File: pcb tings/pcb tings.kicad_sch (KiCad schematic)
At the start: 24 parts, among them SW1 SW_Push, U1 ATmega32U4-A, Y1 16MHz

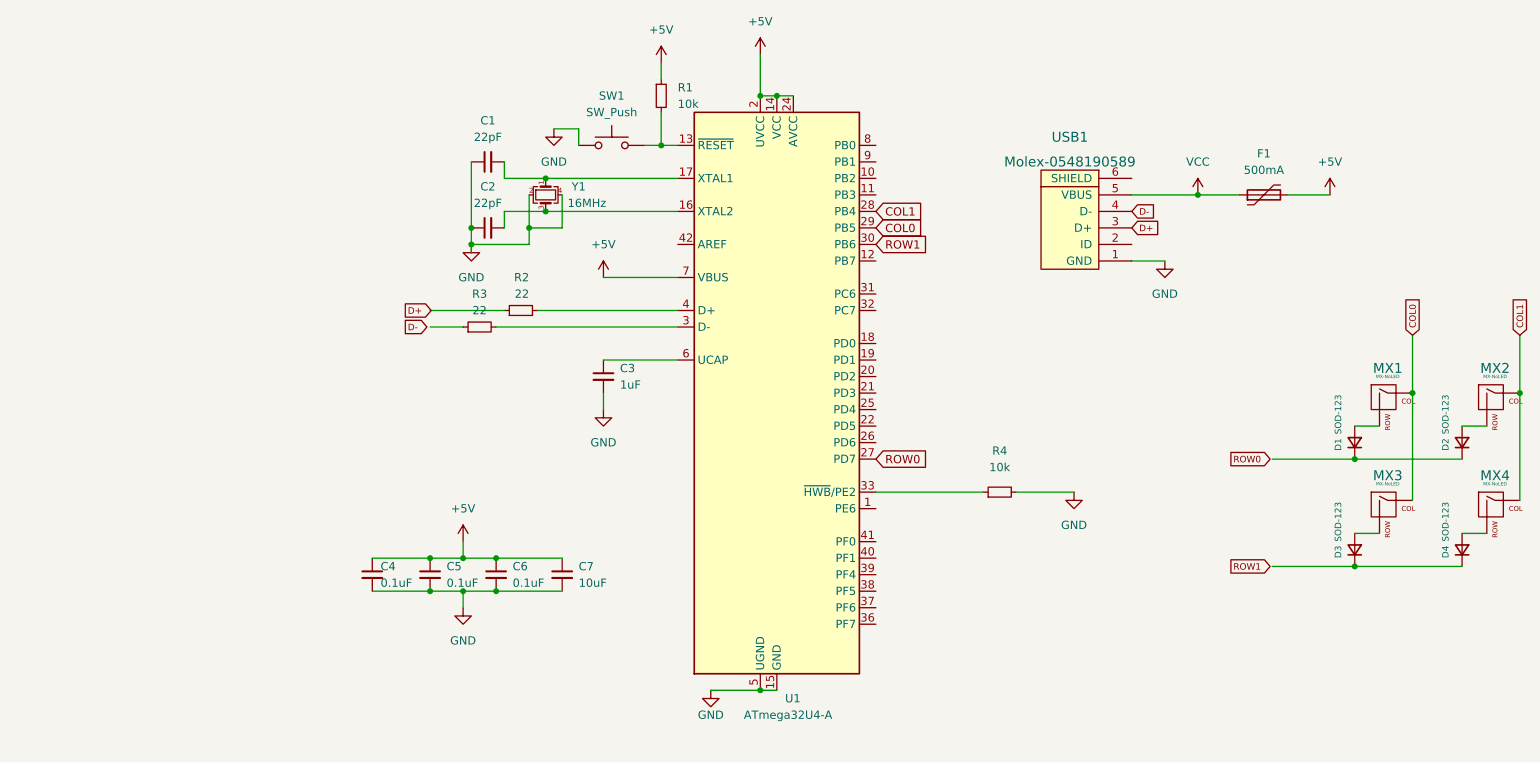
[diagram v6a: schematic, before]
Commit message: fixed connections (ratsnest)
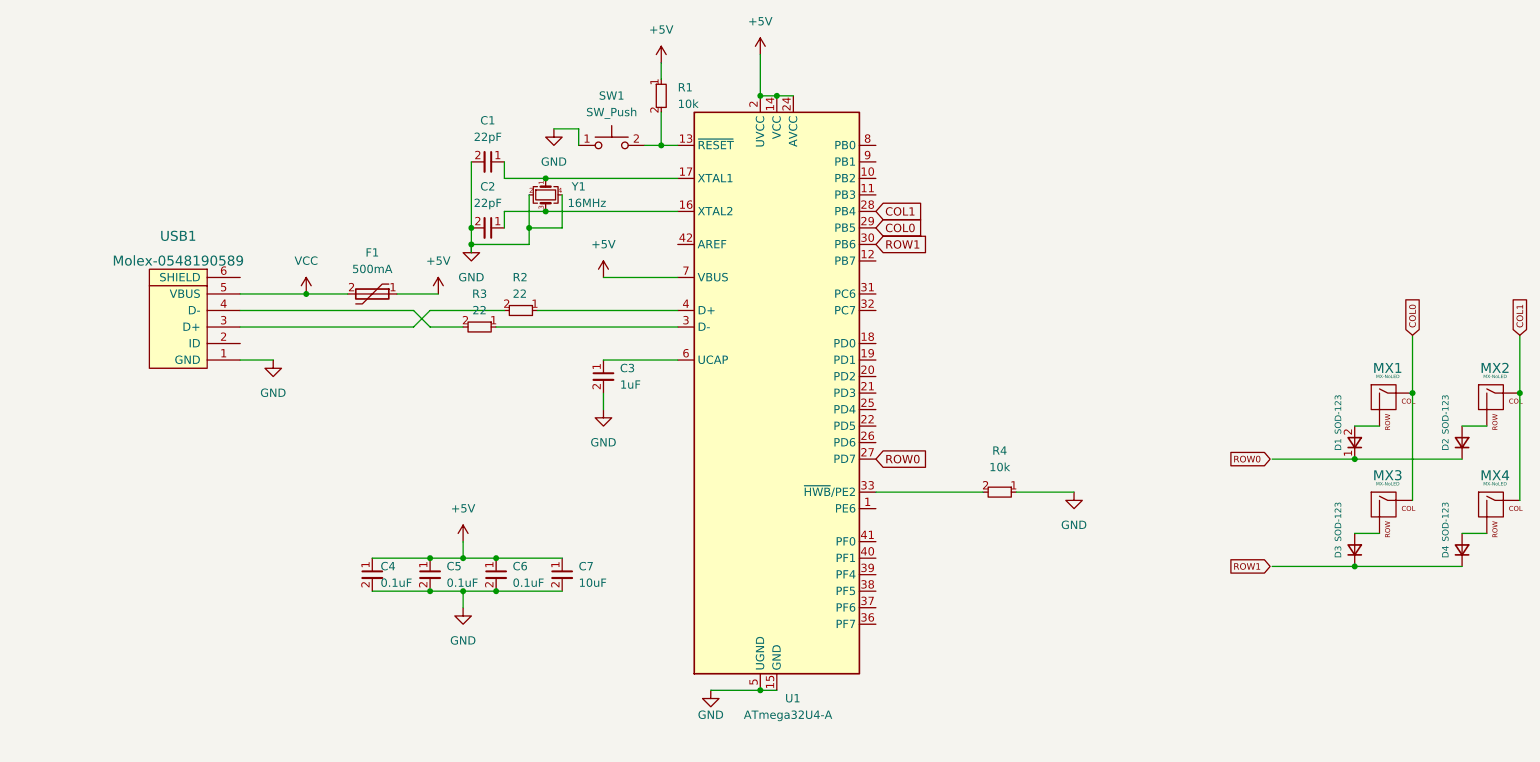
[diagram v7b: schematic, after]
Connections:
- net +5V: now also F1.1; no longer F1.2
- net GND: now also C1.2, C2.2, R4.1; no longer C1.1, C2.1, R4.2
- net VCC: now also F1.2; no longer F1.1
- net at U1.17 (XTAL1), Y1.1: now also C1.1; no longer C1.2
- net at U1.16 (XTAL2), Y1.3: now also C2.1; no longer C2.2
- net at R3.1: now also U1.3 (D-)
- net at R3.2: no longer U1.3 (D-)
- net at R2.1: now also U1.4 (D+)
- net at R2.2: no longer U1.4 (D+)
- net at U1.33 (~{HWB}/PE2): now also R4.2; no longer R4.1
- net D+: no longer names the net of USB1.3 (D+)
- net D-: no longer names the net of USB1.4 (D-)
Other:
- moved on the sheet: USB1

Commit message: Routing
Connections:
- net ROW0: now also D1.1 (K), D2.1 (K)
- net ROW1: now also D3.1 (K), D4.1 (K)
- net D+: now reaches USB1.3 (D+)
- net D+: now also R2.2
- net D-: now reaches USB1.4 (D-)
- net D-: now also R3.2
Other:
- moved on the sheet: F1, USB1
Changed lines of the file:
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@@
   (junction (at 127 48.26) (diameter 0) (color 0 0 0 0)
   )
-  (junction (at 57.15 78.74) (diameter 0) (color 0 0 0 0)
+  (junction (at 44.45 80.01) (diameter 0) (color 0 0 0 0)
   )
   (junction (at 227.33 93.98) (diameter 0) (color 0 0 0 0)
@@
   (junction (at 76.2 124.46) (diameter 0) (color 0 0 0 0)
   )
-  (bus_entry (at 76.2 83.82) (size -2.54 -2.54)
-    (stroke (width 0) (type default) (color 0 0 0 0))
-  )
-  (bus_entry (at 73.66 83.82) (size 2.54 -2.54)
-    (stroke (width 0) (type default) (color 0 0 0 0))
-  )
   (wire (pts (xy 92.71 81.28) (xy 114.3 81.28))
     (stroke (width 0) (type default) (color 0 0 0 0))
@@
     (stroke (width 0) (type default) (color 0 0 0 0))
   )
-  (wire (pts (xy 46.99 78.74) (xy 57.15 78.74))
+  (wire (pts (xy 34.29 80.01) (xy 44.45 80.01))
     (stroke (width 0) (type default) (color 0 0 0 0))
   )
@@
     (stroke (width 0) (type default) (color 0 0 0 0))
   )
-  (wire (pts (xy 46.99 81.28) (xy 73.66 81.28))
-    (stroke (width 0) (type default) (color 0 0 0 0))
-  )
   (wire (pts (xy 111.76 50.8) (xy 111.76 55.88))
     (stroke (width 0) (type default) (color 0 0 0 0))
@@
     (stroke (width 0) (type default) (color 0 0 0 0))
   )
-  (wire (pts (xy 57.15 78.74) (xy 63.5 78.74))
+  (wire (pts (xy 44.45 80.01) (xy 50.8 80.01))
     (stroke (width 0) (type default) (color 0 0 0 0))
   )
@@
     (stroke (width 0) (type default) (color 0 0 0 0))
   )
-  (wire (pts (xy 46.99 83.82) (xy 73.66 83.82))
-    (stroke (width 0) (type default) (color 0 0 0 0))
-  )
   (wire (pts (xy 218.44 120.65) (xy 234.95 120.65))
     (stroke (width 0) (type default) (color 0 0 0 0))
@@
     (stroke (width 0) (type default) (color 0 0 0 0))
   )
-  (wire (pts (xy 71.12 78.74) (xy 77.47 78.74))
+  (wire (pts (xy 58.42 80.01) (xy 64.77 80.01))
     (stroke (width 0) (type default) (color 0 0 0 0))
   )
@@
     (stroke (width 0) (type default) (color 0 0 0 0))
   )
-  (wire (pts (xy 46.99 88.9) (xy 52.07 88.9))
+  (wire (pts (xy 34.29 90.17) (xy 39.37 90.17))
     (stroke (width 0) (type default) (color 0 0 0 0))
   )
@@
   (wire (pts (xy 93.98 60.96) (xy 114.3 60.96))
     (stroke (width 0) (type default) (color 0 0 0 0))
+  )
+  (global_label "D-" (shape input) (at 34.29 82.55 0) (fields_autoplaced)
+    (effects (font (size 1.27 1.27)) (justify left))
+    (property "Intersheet References" "${INTERSHEET_REFS}" (id 0) (at 39.5455 82.4706 0)
+      (effects (font (size 1.27 1.27)) (justify left) hide)
+    )
   )
   (global_label "COL0" (shape input) (at 227.33 85.09 90) (fields_autoplaced)
@@
     )
   )
+  (global_label "D+" (shape input) (at 34.29 85.09 0) (fields_autoplaced)
+    (effects (font (size 1.27 1.27)) (justify left))
+    (property "Intersheet References" "${INTERSHEET_REFS}" (id 0) (at 39.5455 85.0106 0)
+      (effects (font (size 1.27 1.27)) (justify left) hide)
+    )
+  )
   (global_label "ROW0" (shape input) (at 144.78 104.14 0) (fields_autoplaced)
     (effects (font (size 1.27 1.27)) (justify left))
@@
     )
   )
-  (global_label "ROW1" (shape output) (at 199.39 120.65 0) (fields_autoplaced)
-    (effects (font (size 1 1)) (justify left))
-    (property "Intersheet References" "${INTERSHEET_REFS}" (id 0) (at 205.4329 120.5875 0)
-      (effects (font (size 1 1)) (justify left) hide)
-    )
-  )
-  (global_label "ROW0" (shape output) (at 199.39 104.14 0) (fields_autoplaced)
-    (effects (font (size 1 1)) (justify left))
-    (property "Intersheet References" "${INTERSHEET_REFS}" (id 0) (at 205.4329 104.0775 0)
-      (effects (font (size 1 1)) (justify left) hide)
+  (global_label "D-" (shape input) (at 76.2 83.82 180) (fields_autoplaced)
+    (effects (font (size 1.27 1.27)) (justify right))
+    (property "Intersheet References" "${INTERSHEET_REFS}" (id 0) (at 70.9445 83.7406 0)
+      (effects (font (size 1.27 1.27)) (justify right) hide)
+    )
+  )
+  (global_label "ROW1" (shape input) (at 205.74 120.65 180) (fields_autoplaced)
+    (effects (font (size 1 1)) (justify right))
+    (property "Intersheet References" "${INTERSHEET_REFS}" (id 0) (at 199.6971 120.5875 0)
+      (effects (font (size 1 1)) (justify right) hide)
+    )
+  )
+  (global_label "D+" (shape input) (at 76.2 81.28 180) (fields_autoplaced)
+    (effects (font (size 1.27 1.27)) (justify right))
+    (property "Intersheet References" "${INTERSHEET_REFS}" (id 0) (at 70.9445 81.2006 0)
+      (effects (font (size 1.27 1.27)) (justify right) hide)
+    )
+  )
+  (global_label "ROW0" (shape input) (at 205.74 104.14 180) (fields_autoplaced)
+    (effects (font (size 1 1)) (justify right))
+    (property "Intersheet References" "${INTERSHEET_REFS}" (id 0) (at 199.6971 104.0775 0)
+      (effects (font (size 1 1)) (justify right) hide)
     )
   )
@@
     (pin "1")
   )
-  (symbol (lib_id "Device:Polyfuse") (at 67.31 78.74 270) (unit 1)
-    (in_bom yes) (on_board yes) (fields_autoplaced)
-    (property "Reference" "F1" (id 0) (at 67.31 72.39 90))
-    (property "Value" "500mA" (id 1) (at 67.31 74.93 90))
-    (property "Footprint" "Fuse:Fuse_1206_3216Metric" (id 2) (at 62.23 80.01 0)
+  (symbol (lib_id "Device:Polyfuse") (at 54.61 80.01 270) (unit 1)
+    (in_bom yes) (on_board yes) (fields_autoplaced)
+    (property "Reference" "F1" (id 0) (at 54.61 73.66 90))
+    (property "Value" "500mA" (id 1) (at 54.61 76.2 90))
+    (property "Footprint" "Fuse:Fuse_1206_3216Metric" (id 2) (at 49.53 81.28 0)
       (effects (font (size 1.27 1.27)) (justify left) hide)
     )
-    (property "Datasheet" "~" (id 3) (at 67.31 78.74 0)
+    (property "Datasheet" "~" (id 3) (at 54.61 80.01 0)
       (effects (font (size 1.27 1.27)) hide)
     )
@@
     (pin "4")
   )
-  (symbol (lib_id "power:+5V") (at 77.47 78.74 0) (unit 1)
-    (in_bom yes) (on_board yes) (fields_autoplaced)
-    (property "Reference" "#PWR05" (id 0) (at 77.47 82.55 0)
-      (effects (font (size 1.27 1.27)) hide)
-    )
-    (property "Value" "+5V" (id 1) (at 77.47 73.66 0))
-    (property "Footprint" "" (id 2) (at 77.47 78.74 0)
-      (effects (font (size 1.27 1.27)) hide)
-    )
-    (property "Datasheet" "" (id 3) (at 77.47 78.74 0)
-      (effects (font (size 1.27 1.27)) hide)
-    )
-    (pin "1")
-  )
-  (symbol (lib_id "power:VCC") (at 57.15 78.74 0) (unit 1)
-    (in_bom yes) (on_board yes) (fields_autoplaced)
-    (property "Reference" "#PWR04" (id 0) (at 57.15 82.55 0)
-      (effects (font (size 1.27 1.27)) hide)
-    )
-    (property "Value" "VCC" (id 1) (at 57.15 73.66 0))
-    (property "Footprint" "" (id 2) (at 57.15 78.74 0)
-      (effects (font (size 1.27 1.27)) hide)
-    )
-    (property "Datasheet" "" (id 3) (at 57.15 78.74 0)
+  (symbol (lib_id "power:+5V") (at 64.77 80.01 0) (unit 1)
+    (in_bom yes) (on_board yes) (fields_autoplaced)
+    (property "Reference" "#PWR05" (id 0) (at 64.77 83.82 0)
+      (effects (font (size 1.27 1.27)) hide)
+    )
+    (property "Value" "+5V" (id 1) (at 64.77 74.93 0))
+    (property "Footprint" "" (id 2) (at 64.77 80.01 0)
+      (effects (font (size 1.27 1.27)) hide)
+    )
+    (property "Datasheet" "" (id 3) (at 64.77 80.01 0)
+      (effects (font (size 1.27 1.27)) hide)
+    )
+    (pin "1")
+  )
+  (symbol (lib_id "power:VCC") (at 44.45 80.01 0) (unit 1)
+    (in_bom yes) (on_board yes) (fields_autoplaced)
+    (property "Reference" "#PWR04" (id 0) (at 44.45 83.82 0)
+      (effects (font (size 1.27 1.27)) hide)
+    )
+    (property "Value" "VCC" (id 1) (at 44.45 74.93 0))
+    (property "Footprint" "" (id 2) (at 44.45 80.01 0)
+      (effects (font (size 1.27 1.27)) hide)
+    )
+    (property "Datasheet" "" (id 3) (at 44.45 80.01 0)
       (effects (font (size 1.27 1.27)) hide)
     )
@@
     (pin "2")
   )
-  (symbol (lib_id "random-keyboard-parts:Molex-0548190589") (at 39.37 83.82 90) (unit 1)
-    (in_bom yes) (on_board yes) (fields_autoplaced)
-    (property "Reference" "USB1" (id 0) (at 37.465 69.85 90)
+  (symbol (lib_id "random-keyboard-parts:Molex-0548190589") (at 26.67 85.09 90) (unit 1)
+    (in_bom yes) (on_board yes) (fields_autoplaced)
+    (property "Reference" "USB1" (id 0) (at 24.765 71.12 90)
       (effects (font (size 1.524 1.524)))
     )
-    (property "Value" "Molex-0548190589" (id 1) (at 37.465 73.66 90)
+    (property "Value" "Molex-0548190589" (id 1) (at 24.765 74.93 90)
       (effects (font (size 1.524 1.524)))
     )
-    (property "Footprint" "random-keyboard-parts:Molex-0548190589" (id 2) (at 39.37 83.82 0)
-      (effects (font (size 1.524 1.524)) hide)
-    )
-    (property "Datasheet" "" (id 3) (at 39.37 83.82 0)
+    (property "Footprint" "random-keyboard-parts:Molex-0548190589" (id 2) (at 26.67 85.09 0)
+      (effects (font (size 1.524 1.524)) hide)
+    )
+    (property "Datasheet" "" (id 3) (at 26.67 85.09 0)
       (effects (font (size 1.524 1.524)) hide)
     )
@@
     (pin "2")
   )
-  (symbol (lib_id "power:GND") (at 52.07 88.9 0) (unit 1)
-    (in_bom yes) (on_board yes) (fields_autoplaced)
-    (property "Reference" "#PWR07" (id 0) (at 52.07 95.25 0)
-      (effects (font (size 1.27 1.27)) hide)
-    )
-    (property "Value" "GND" (id 1) (at 52.07 93.98 0))
-    (property "Footprint" "" (id 2) (at 52.07 88.9 0)
-      (effects (font (size 1.27 1.27)) hide)
-    )
-    (property "Datasheet" "" (id 3) (at 52.07 88.9 0)
-      (effects (font (size 1.27 1.27)) hide)
-    )
+  (symbol (lib_id "power:GND") (at 39.37 90.17 0) (unit 1)
+    (in_bom yes) (on_board yes) (fields_autoplaced)
+    (property "Reference" "#PWR07" (id 0) (at 39.37 96.52 0)
+      (effects (font (size 1.27 1.27)) hide)
+    )
+    (property "Value" "GND" (id 1) (at 39.37 95.25 0))
+    (property "Footprint" "" (id 2) (at 39.37 90.17 0)
+      (effects (font (size 1.27 1.27)) hide)
+    )
+    (property "Datasheet" "" (id 3) (at 39.37 90.17 0)
+      (effects (font (size 1.27 1.27)) hide)
+    )
